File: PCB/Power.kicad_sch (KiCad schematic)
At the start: 17 parts, among them SW2 SW_SPST, U2 XC6210B332MR, U3 BQ25185DLHR

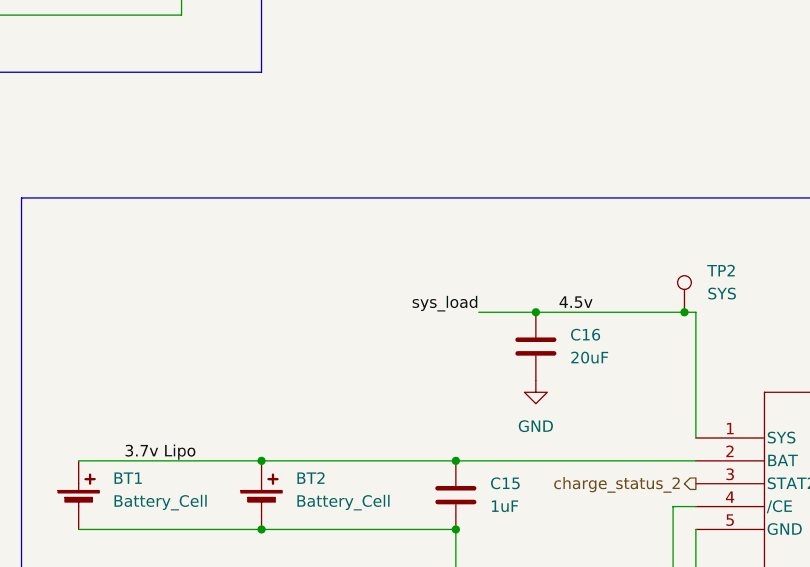
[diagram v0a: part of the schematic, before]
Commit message: Added toggle switch SPDT
Add switch to turn system on and off, also used LibaryLoader
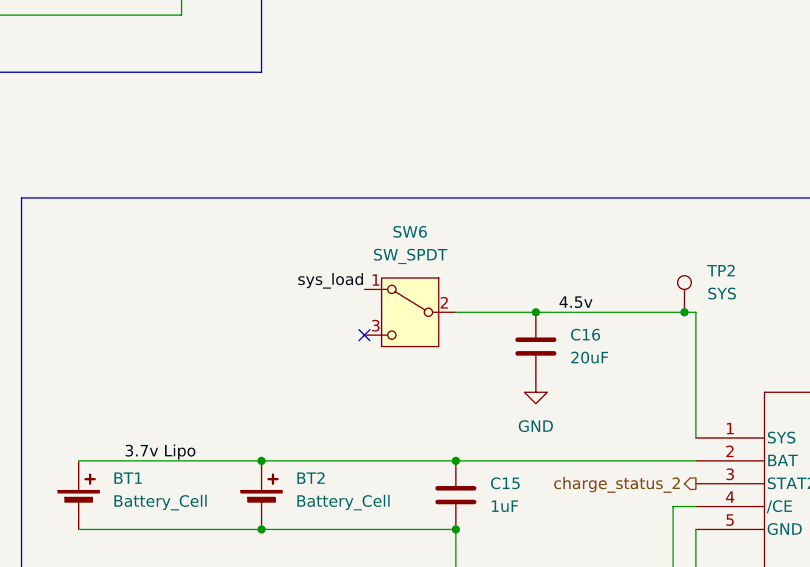
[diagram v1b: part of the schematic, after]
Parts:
- added SW6: SW_SPDT, LibraryLoader:SS12D11G5R, symbol Switch:SW_SPDT
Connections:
- net 4.5v: now also SW6.2 (B); no longer C13.1, SW2.1 (A), U2.1 (VIN)
- new net sys_load: C13.1, SW2.1 (A), SW6.1 (A), U2.1 (VIN)
- no-connect marks 0 -> 1
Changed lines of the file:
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@@
 		(color 0 0 0 0)
 	)
+	(no_connect
+		(at 125.73 96.52)
+	)
 	(wire
 		(pts
@@
 	(wire
 		(pts
-			(xy 138.43 93.98) (xy 144.78 93.98)
+			(xy 135.89 93.98) (xy 144.78 93.98)
 		)
 		(stroke
@@
 	)
 	(label "sys_load"
-		(at 138.43 93.98 180)
+		(at 125.73 91.44 180)
 		(effects
 			(font
@@
 					(unit 1)
 				)
+			)
+		)
+	)
+	(symbol
+		(lib_id "Switch:SW_SPDT")
+		(at 130.81 93.98 0)
+		(mirror y)
+		(unit 1)
+		(exclude_from_sim no)
+		(in_bom yes)
+		(on_board yes)
+		(dnp no)
+		(fields_autoplaced yes)
+		(property "Reference" "SW6"
+			(at 130.81 85.09 0)
+			(effects
+				(font
+					(size 1.27 1.27)
+				)
+			)
+		)
+		(property "Value" "SW_SPDT"
+			(at 130.81 87.63 0)
+			(effects
+				(font
+					(size 1.27 1.27)
+				)
+			)
+		)
+		(property "Footprint" "LibraryLoader:SS12D11G5R"
+			(at 130.81 93.98 0)
+			(effects
+				(font
+					(size 1.27 1.27)
+				)
+				(hide yes)
+			)
+		)
+		(property "Datasheet" "https://jlcpcb.com/api/file/downloadByFileSystemAccessId/8588892087853469696"
+			(at 130.81 101.6 0)
+			(effects
+				(font
+					(size 1.27 1.27)
+				)
+				(hide yes)
+			)
+		)
+		(property "Description" "Switch, single pole double throw"
+			(at 130.81 93.98 0)
+			(effects
+				(font
+					(size 1.27 1.27)
+				)
+				(hide yes)
+			)
+		)
+		(property "JLCPCB Part #" "C388633"
+			(at 130.81 93.98 0)
+			(effects
+				(font
+					(size 1.27 1.27)
+				)
+				(hide yes)
+			)
+		)
+		(pin "2"
+		)
+		(pin "3"
+		)
+		(pin "1"
+		)
+		(instances
+			(project ""
+				(path "/a8261359-6329-4960-96c7-d82fbb91cdcc/dcce5b57-fd6b-4d93-a9df-9259f2d6944b"
+					(reference "SW6")
+					(unit 1)
+				)
